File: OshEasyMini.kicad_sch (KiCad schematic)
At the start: 119 parts, among them J1 TAGCONNECT, J10 Conn_01x04_MountingPin, J3 SMA_Edgelaunch, J4 PYROS, J5 UFL, J6 BAT, Q1 SiA449DJ, Q2 AO3400A, Q3 SiA449DJ, U1 MIA-M10Q, U11 CPT-7502-65-SMT-TR, U12 LM293QT, U17 MCP73831-2-OT, U18 TC2185-3.3VxCTTR, U19 W25Q64JVXGIQ, U2 WE-TVS-82400102, U20 SISB46DN, U21 SN74LVC1G80QDCKTQ1, U3 ADXL375, U4 MS5607-02BA, U6 MCP130-xxxxTT, U7 DRV5012AEDMRR, U8 CC1200, U9 ATSAMD21G17D-A, X2 ECS-160-8-36Q-AES-TR1, Y1 40mhz 8pF 30 Ohms, Y2 32.768khz

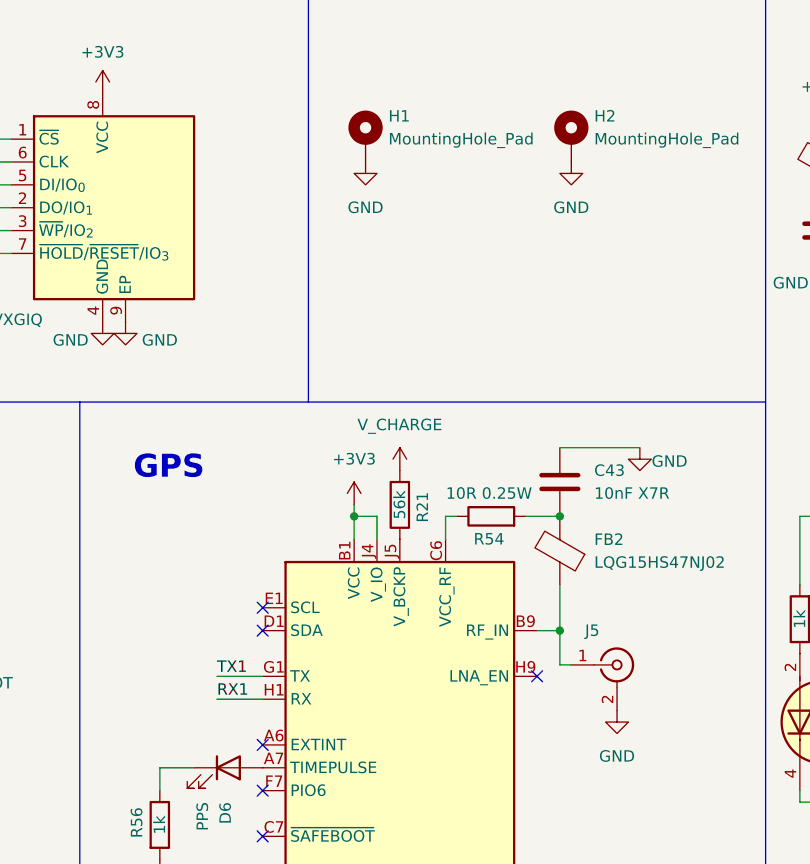
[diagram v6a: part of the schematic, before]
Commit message: CRITICAL: GPS UART RX/TX swapped. Fixed.
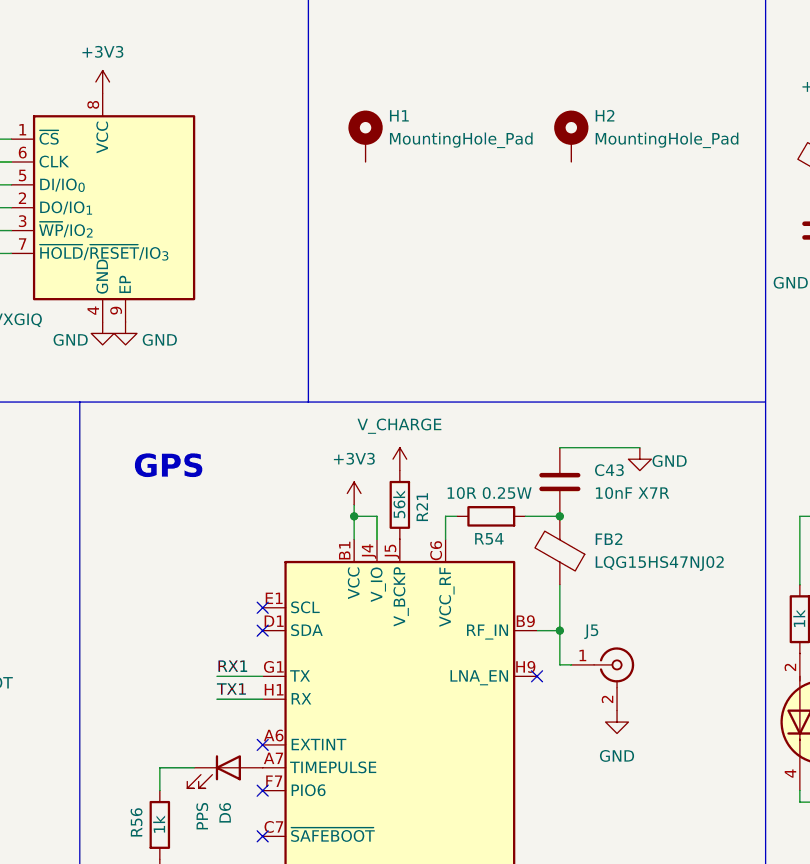
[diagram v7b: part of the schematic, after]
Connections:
- net GND: no longer H1.1, H2.1
- net RX1: now also U1.G1 (TX); no longer U1.H1 (RX)
- net TX1: now also U1.H1 (RX); no longer U1.G1 (TX)
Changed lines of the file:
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@@
 		(title "MetrumITX")
 		(date "2025-12-19")
-		(rev "v1.0")
+		(rev "v1.1")
 		(company "Leviathan Flight Systems")
 		(comment 1 "Copyright 2025 by Bdale Garbee")
@@
 		)
 	)
+	(label "TX1"
+		(at 142.24 236.22 0)
+		(effects
+			(font
+				(size 1.27 1.27)
+			)
+			(justify left bottom)
+		)
+	)
 	(label "SCK5"
 		(at 316.23 96.52 0)
@@
 		)
 	)
-	(label "TX1"
-		(at 142.24 233.68 0)
-		(effects
-			(font
-				(size 1.27 1.27)
-			)
-			(justify left bottom)
-		)
-	)
 	(label "FIRE_A"
 		(at 265.43 236.22 0)
@@
 		)
 	)
-	(label "PH1"
-		(at 262.89 226.06 0)
+	(label "RX1"
+		(at 142.24 233.68 0)
 		(effects
 			(font
@@
 		)
 	)
-	(label "MGSW_IN"
-		(at 12.7 114.3 0)
+	(label "PH1"
+		(at 262.89 226.06 0)
 		(effects
 			(font
@@
 		)
 	)
-	(label "PH1"
-		(at 345.44 227.33 0)
+	(label "MGSW_IN"
+		(at 12.7 114.3 0)
 		(effects
 			(font
@@
 		)
 	)
-	(label "RX1"
-		(at 142.24 236.22 0)
+	(label "PH1"
+		(at 345.44 227.33 0)
 		(effects
 			(font
@@
 	)
 	(symbol
-		(lib_id "power:GND")
-		(at 158.75 176.53 0)
-		(unit 1)
-		(exclude_from_sim no)
-		(in_bom yes)
-		(on_board yes)
-		(dnp no)
-		(fields_autoplaced yes)
-		(property "Reference" "#PWR016"
-			(at 158.75 182.88 0)
-			(effects
-				(font
-					(size 1.27 1.27)
-				)
-				(hide yes)
-			)
-		)
-		(property "Value" "GND"
-			(at 158.75 181.61 0)
-			(effects
-				(font
-					(size 1.27 1.27)
-				)
-			)
-		)
-		(property "Footprint" ""
-			(at 158.75 176.53 0)
-			(effects
-				(font
-					(size 1.27 1.27)
-				)
-				(hide yes)
-			)
-		)
-		(property "Datasheet" ""
-			(at 158.75 176.53 0)
-			(effects
-				(font
-					(size 1.27 1.27)
-				)
-				(hide yes)
-			)
-		)
-		(property "Description" "Power symbol creates a global label with name \"GND\" , ground"
-			(at 158.75 176.53 0)
-			(effects
-				(font
-					(size 1.27 1.27)
-				)
-				(hide yes)
-			)
-		)
-		(pin "1"
-		)
-		(instances
-			(project "OshEasyMini"
-				(path "/dd7a172f-a780-496c-a5d6-72309e0b3597"
-					(reference "#PWR016")
-					(unit 1)
-				)
-			)
-		)
-	)
-	(symbol
 		(lib_id "power:+3V3")
 		(at 280.67 218.44 0)
@@
 					(unit 1)
 				)
-			)
-		)
-	)
-	(symbol
-		(lib_id "power:GND")
-		(at 181.61 176.53 0)
-		(unit 1)
-		(exclude_from_sim no)
-		(in_bom yes)
-		(on_board yes)
-		(dnp no)
-		(fields_autoplaced yes)
-		(property "Reference" "#PWR028"
-			(at 181.61 182.88 0)
-			(effects
-				(font
-					(size 1.27 1.27)
-				)
-				(hide yes)
-			)
-		)
-		(property "Value" "GND"
-			(at 181.61 181.61 0)
-			(effects
-				(font
-					(size 1.27 1.27)
-				)
-			)
-		)
-		(property "Footprint" ""
-			(at 181.61 176.53 0)
-			(effects
-				(font
-					(size 1.27 1.27)
-				)
-				(hide yes)
-			)
-		)
-		(property "Datasheet" ""
-			(at 181.61 176.53 0)
-			(effects
-				(font
-					(size 1.27 1.27)
-				)
-				(hide yes)
-			)
-		)
-		(property "Description" "Power symbol creates a global label with name \"GND\" , ground"
-			(at 181.61 176.53 0)
-			(effects
-				(font
-					(size 1.27 1.27)
-				)
-				(hide yes)
-			)
-		)
-		(pin "1"
-		)
-		(instances
-			(project "OshEasyMini"
-				(path "/dd7a172f-a780-496c-a5d6-72309e0b3597"
-					(reference "#PWR028")
-					(unit 1)
-				)
